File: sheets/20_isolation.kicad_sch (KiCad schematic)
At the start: 0 parts

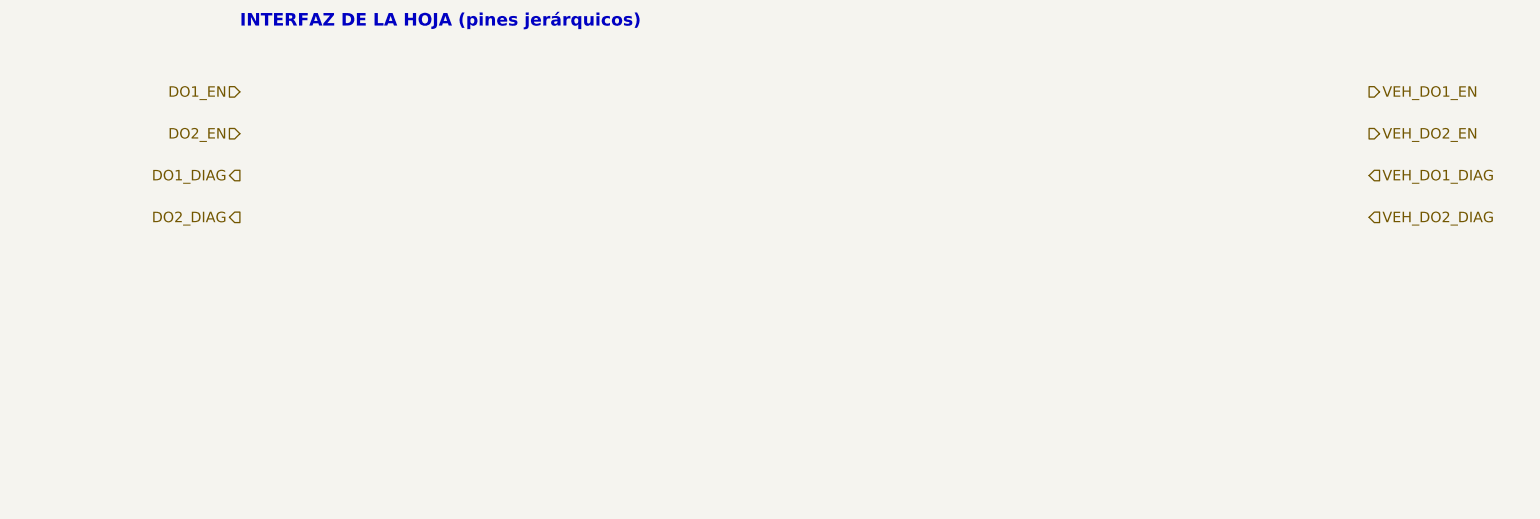
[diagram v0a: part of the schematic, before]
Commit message: 70_output: salida low-side con latch y señal PWR_FLT
- 70_output (DO1/DO2): MOSFET FDD7N25LZ (demo, 250 V) con TVS SMCJ188A
  en el drenador, latch de sobrecorriente a ~0.7 A (R 1 ohm + BC817/BC807,
  rearme con EN=0), apagado del gate por PWR_FLT_N o latch (BAT54A) y
  DIAG por divisor del drenador con zener 5V1. OUT pasa a pasivo.
- Jerarquía: VEH_PWR_FLT_N de 10_power_input a 70_output y 20_isolation;
  PWR_FLT de 20_isolation a 40_mcu (KW45 y ESP32-S3).
- 10_power_input: solo interfaz (VEH_DO1/2 pasivos, VEH_PWR_FLT_N);
  el circuito con LM74930 va en un commit aparte.
- CLAUDE.md: procedimiento para componentes fuera de las librerías.
- README: 70_output es low-side.

Co-Authored-By: Claude Opus 5.5 <noreply@anthropic.com>
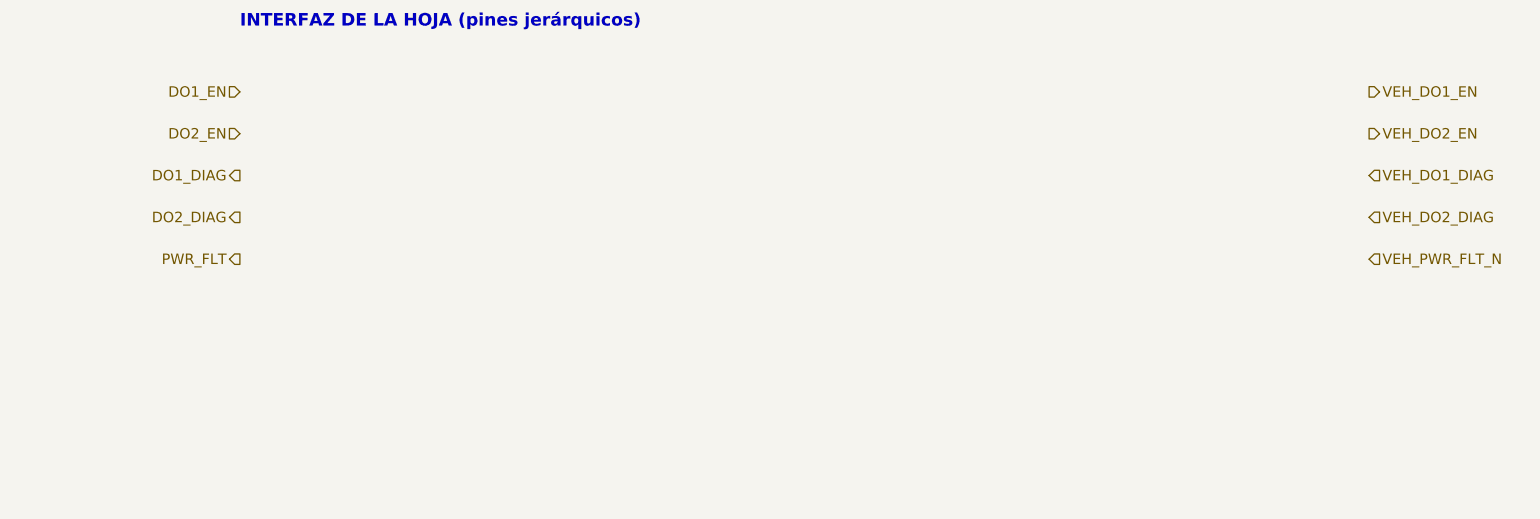
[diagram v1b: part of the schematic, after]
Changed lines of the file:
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@@
+		)
+	)
+	(hierarchical_label "VEH_PWR_FLT_N"
+		(shape input)
+		(at 375.92 50.8 0)
+		(effects
+			(font
+				(size 1.27 1.27)
+			)
+			(justify left)
+		)
+	)
+	(hierarchical_label "PWR_FLT"
+		(shape output)
+		(at 238.76 50.8 180)
+		(effects
+			(font
+				(size 1.27 1.27)
+			)
+			(justify right)
 		)
 	)

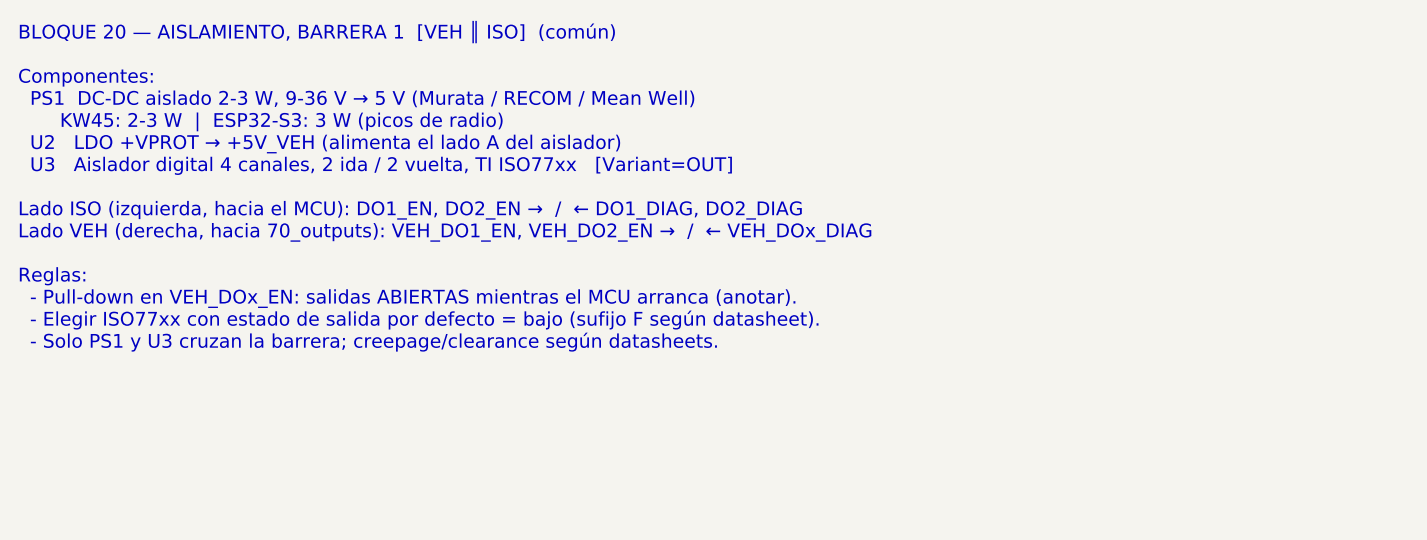
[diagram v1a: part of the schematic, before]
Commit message: Alcance: solo ESP32-S3, CAN clásico por TWAI, sin MCP2518FD
- Raíz: el bloque 40_mcu apunta a 40_mcu_esp32s3. 40_mcu_kw45 queda en
  el repo solo como referencia, fuera de la jerarquía.
- CAN: se eliminan el MCP2518FD, el cristal y los pines CANFD_SCK/MOSI/
  MISO, CS_CAN e INT_CAN en 60_can, 40_mcu_esp32s3 y la raíz (etiquetas,
  cables y pines de hoja). TWAI nativo (J1939) directo al ADM3055E.
  Se quita la variante CANFD.
- 20_isolation (nota): PS1 >= 5 W y entrada 9-72 V (corte OV 38.4 V);
  U2 = TPS7A1650-Q1 para +5V_VEH.
- 40_mcu_esp32s3 (nota): desacople 22 uF + 100 nF según Espressif y
  límite de 47 uF en +3V3_D por el TPS62A02-Q1; solo BLE en operación.
- README: tabla corregida (LM74930-Q1 en 10_power_input, 20, 30, 40, 60),
  sección MCU y "Requisitos para el firmware" (rearme del latch >= 100 ms,
  arranque limpio tras brownout, NimBLE con WiFi desactivado).
- CLAUDE.md: sección "Alcance" (ESP32-S3 único, dimensionar con WiFi).

ERC: 180 -> 160 violaciones; sin errores nuevos. Las restantes son de
hojas sin terminar (20, 30, 60) y etiquetas de la raíz sin destino.

Co-Authored-By: Claude Opus 5.5 <noreply@anthropic.com>
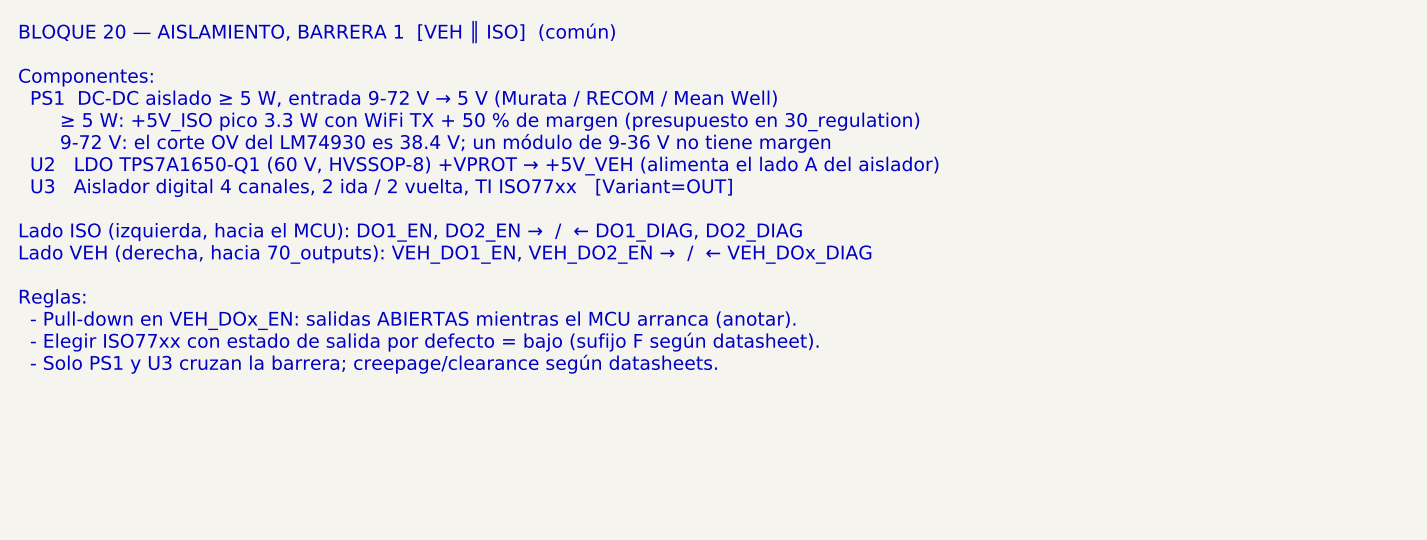
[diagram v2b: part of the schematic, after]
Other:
- note added: "BLOQUE 20 — AISLAMIENTO, BARRERA 1 [VEH ║ ISO] (común) Componentes: PS1 DC-DC aislado ≥ 5 W, entrada 9-72 V → 5 V (Murata / RECOM / Mean Well) ≥ 5 W: +5V_ISO pico 3.3 W con WiFi TX + 50 % de margen (presupuesto en 30_regulation) 9-72 V: el corte OV del LM74930 es 38.4 V; un módulo de 9-36 V no tiene margen U2 LDO TPS7A1650-Q1 (60 V, HVSSOP-8) +VPROT → +5V_VEH (alimenta el lado A del aislador) U3 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"
- note removed: "BLOQUE 20 — AISLAMIENTO, BARRERA 1 [VEH ║ ISO] (común) Componentes: PS1 DC-DC aislado 2-3 W, 9-36 V → 5 V (Murata / RECOM / Mean Well) KW45: 2-3 W | ESP32-S3: 3 W (picos de radio) U2 LDO +VPROT → +5V_VEH (alimenta el lado A del aislador) U3 Aislador digital 4 canales, 2 ida / 2 vuelta, TI ISO77xx [Variant=OUT] Lado ISO (izquierda, hacia el MCU): DO1_EN, DO2_EN → / ← DO1_DIAG, DO2_DIAG Lado VEH (d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"
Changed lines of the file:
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@@
 		)
 	)
-	(text "BLOQUE 20 — AISLAMIENTO, BARRERA 1  [VEH ║ ISO]  (común)\n\nComponentes:\n  PS1  DC-DC aislado 2-3 W, 9-36 V → 5 V (Murata / RECOM / Mean Well)\n       KW45: 2-3 W  |  ESP32-S3: 3 W (picos de radio)\n  U2   LDO +VPROT → +5V_VEH (alimenta el lado A del aislador)\n  U3   Aislador digital 4 canales, 2 ida / 2 vuelta, TI ISO77xx   [Variant=OUT]\n\nLado ISO (izquierda, hacia el MCU): DO1_EN, DO2_EN →  /  ← DO1_DIAG, DO2_DIAG\nLado VEH (derecha, hacia 70_outputs): VEH_DO1_EN, VEH_DO2_EN →  /  ← VEH_DOx_DIAG\n\nReglas:\n  - Pull-down en VEH_DOx_EN: salidas ABIERTAS mientras el MCU arranca (anotar).\n  - Elegir ISO77xx con estado de salida por defecto = bajo (sufijo F según datasheet).\n  - Solo PS1 y U3 cruzan la barrera; creepage/clearance según datasheets."
+	(text "BLOQUE 20 — AISLAMIENTO, BARRERA 1  [VEH ║ ISO]  (común)\n\nComponentes:\n  PS1  DC-DC aislado ≥ 5 W, entrada 9-72 V → 5 V (Murata / RECOM / Mean Well)\n       ≥ 5 W: +5V_ISO pico 3.3 W con WiFi TX + 50 % de margen (presupuesto en 30_regulation)\n       9-72 V: el corte OV del LM74930 es 38.4 V; un módulo de 9-36 V no tiene margen\n  U2   LDO TPS7A1650-Q1 (60 V, HVSSOP-8) +VPROT → +5V_VEH (alimenta el lado A del aislador)\n  U3   Aislador digital 4 canales, 2 ida / 2 vuelta, TI ISO77xx   [Variant=OUT]\n\nLado ISO (izquierda, hacia el MCU): DO1_EN, DO2_EN →  /  ← DO1_DIAG, DO2_DIAG\nLado VEH (derecha, hacia 70_outputs): VEH_DO1_EN, VEH_DO2_EN →  /  ← VEH_DOx_DIAG\n\nReglas:\n  - Pull-down en VEH_DOx_EN: salidas ABIERTAS mientras el MCU arranca (anotar).\n  - Elegir ISO77xx con estado de salida por defecto = bajo (sufijo F según datasheet).\n  - Solo PS1 y U3 cruzan la barrera; creepage/clearance según datasheets."
 		(exclude_from_sim no)
 		(at 20.32 20.32 0)
@@
 		)
 	)
+	(hierarchical_label "PWR_FLT"
+		(shape output)
+		(at 238.76 50.8 180)
+		(effects
+			(font
+				(size 1.27 1.27)
+			)
+			(justify right)
+		)
+	)
 	(hierarchical_label "DO2_EN"
 		(shape input)
@@
 		(shape input)
 		(at 375.92 40.64 0)
+		(effects
+			(font
+				(size 1.27 1.27)
+			)
+			(justify left)
+		)
+	)
+	(hierarchical_label "VEH_PWR_FLT_N"
+		(shape input)
+		(at 375.92 50.8 0)
 		(effects
 			(font
@@
 		)
 	)
-	(hierarchical_label "VEH_PWR_FLT_N"
-		(shape input)
-		(at 375.92 50.8 0)
-		(effects
-			(font
-				(size 1.27 1.27)
-			)
-			(justify left)
-		)
-	)
-	(hierarchical_label "PWR_FLT"
-		(shape output)
-		(at 238.76 50.8 180)
-		(effects
-			(font
-				(size 1.27 1.27)
-			)
-			(justify right)
-		)
-	)

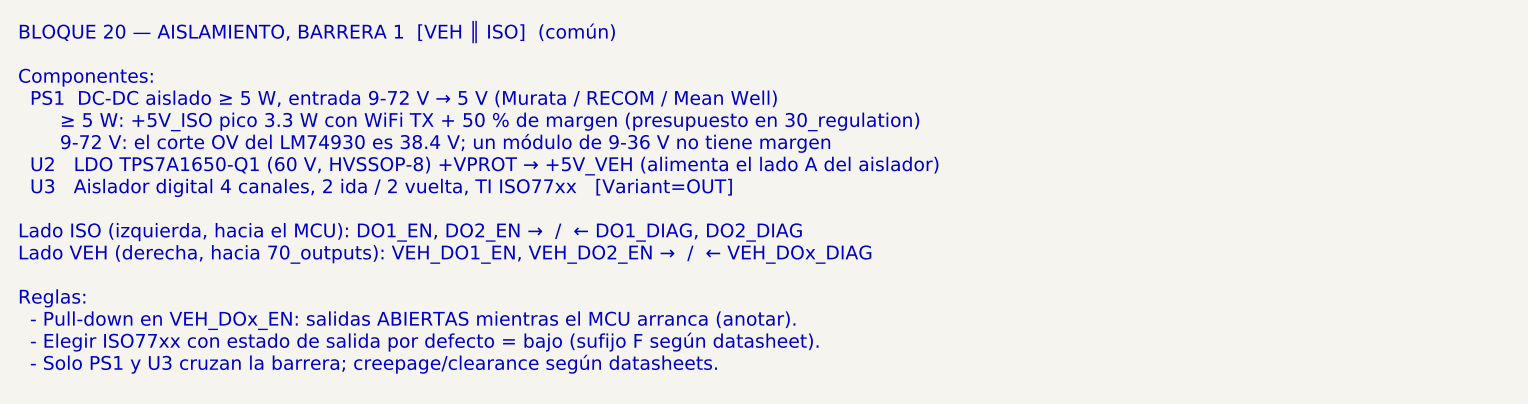
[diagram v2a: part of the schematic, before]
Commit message: ADM3055E: consumo de VCC confirmado con el datasheet Rev. D
- ICC en dominante con RL = 60 ohm: 180 mA típ / 260 mA máx (tabla 1);
  IIO 3.6 / 5 mA. Anotado en 60_can.
- +5V_ISO pico: 0.26 A (ADM3055E) + 0.39 A (buck, 521 mA en +3V3_D con
  WiFi TX) + 0.02 A (LDO) = 3.35 W; x1.5 = 5.0 W. PS1 se mantiene en
  >= 5 W (no hace falta 6 W). Nota de 20_isolation actualizada.
- docs/datasheets/adm3055e-adm3057e.pdf.

Co-Authored-By: Claude Opus 5.5 <noreply@anthropic.com>
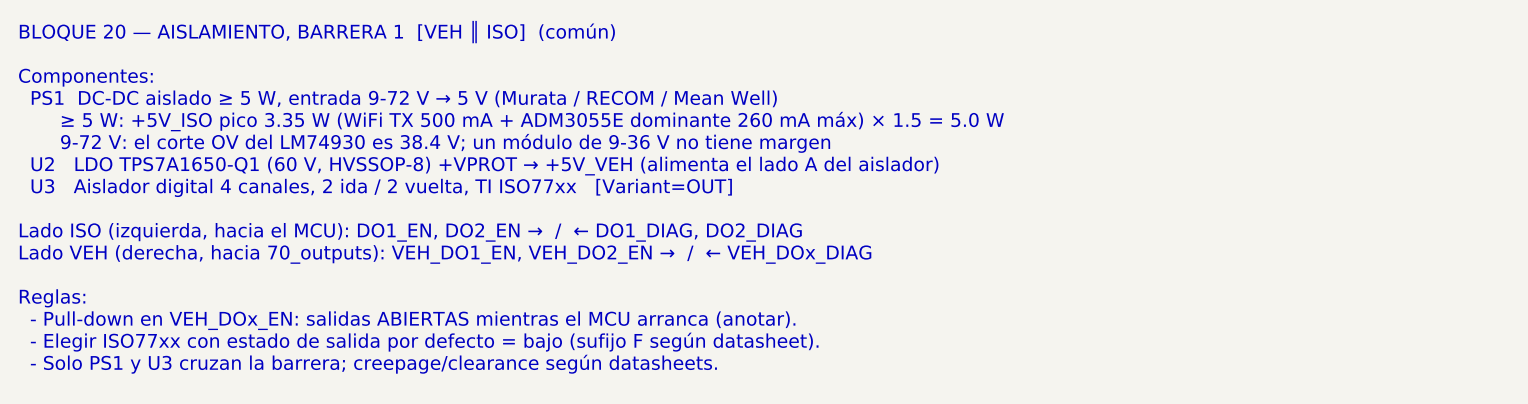
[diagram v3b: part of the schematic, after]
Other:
- note added: "BLOQUE 20 — AISLAMIENTO, BARRERA 1 [VEH ║ ISO] (común) Componentes: PS1 DC-DC aislado ≥ 5 W, entrada 9-72 V → 5 V (Murata / RECOM / Mean Well) ≥ 5 W: +5V_ISO pico 3.35 W (WiFi TX 500 mA + ADM3055E dominante 260 mA máx) × 1.5 = 5.0 W 9-72 V: el corte OV del LM74930 es 38.4 V; un módulo de 9-36 V no tiene margen U2 LDO TPS7A1650-Q1 (60 V, HVSSOP-8) +VPROT → +5V_VEH (alimenta el lado A del aislador)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"
- note removed: "BLOQUE 20 — AISLAMIENTO, BARRERA 1 [VEH ║ ISO] (común) Componentes: PS1 DC-DC aislado ≥ 5 W, entrada 9-72 V → 5 V (Murata / RECOM / Mean Well) ≥ 5 W: +5V_ISO pico 3.3 W con WiFi TX + 50 % de margen (presupuesto en 30_regulation) 9-72 V: el corte OV del LM74930 es 38.4 V; un módulo de 9-36 V no tiene margen U2 LDO TPS7A1650-Q1 (60 V, HVSSOP-8) +VPROT → +5V_VEH (alimenta el lado A del aislador) U3 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"
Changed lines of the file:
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@@
 		)
 	)
-	(text "BLOQUE 20 — AISLAMIENTO, BARRERA 1  [VEH ║ ISO]  (común)\n\nComponentes:\n  PS1  DC-DC aislado ≥ 5 W, entrada 9-72 V → 5 V (Murata / RECOM / Mean Well)\n       ≥ 5 W: +5V_ISO pico 3.3 W con WiFi TX + 50 % de margen (presupuesto en 30_regulation)\n       9-72 V: el corte OV del LM74930 es 38.4 V; un módulo de 9-36 V no tiene margen\n  U2   LDO TPS7A1650-Q1 (60 V, HVSSOP-8) +VPROT → +5V_VEH (alimenta el lado A del aislador)\n  U3   Aislador digital 4 canales, 2 ida / 2 vuelta, TI ISO77xx   [Variant=OUT]\n\nLado ISO (izquierda, hacia el MCU): DO1_EN, DO2_EN →  /  ← DO1_DIAG, DO2_DIAG\nLado VEH (derecha, hacia 70_outputs): VEH_DO1_EN, VEH_DO2_EN →  /  ← VEH_DOx_DIAG\n\nReglas:\n  - Pull-down en VEH_DOx_EN: salidas ABIERTAS mientras el MCU arranca (anotar).\n  - Elegir ISO77xx con estado de salida por defecto = bajo (sufijo F según datasheet).\n  - Solo PS1 y U3 cruzan la barrera; creepage/clearance según datasheets."
+	(text "BLOQUE 20 — AISLAMIENTO, BARRERA 1  [VEH ║ ISO]  (común)\n\nComponentes:\n  PS1  DC-DC aislado ≥ 5 W, entrada 9-72 V → 5 V (Murata / RECOM / Mean Well)\n       ≥ 5 W: +5V_ISO pico 3.35 W (WiFi TX 500 mA + ADM3055E dominante 260 mA máx) × 1.5 = 5.0 W\n       9-72 V: el corte OV del LM74930 es 38.4 V; un módulo de 9-36 V no tiene margen\n  U2   LDO TPS7A1650-Q1 (60 V, HVSSOP-8) +VPROT → +5V_VEH (alimenta el lado A del aislador)\n  U3   Aislador digital 4 canales, 2 ida / 2 vuelta, TI ISO77xx   [Variant=OUT]\n\nLado ISO (izquierda, hacia el MCU): DO1_EN, DO2_EN →  /  ← DO1_DIAG, DO2_DIAG\nLado VEH (derecha, hacia 70_outputs): VEH_DO1_EN, VEH_DO2_EN →  /  ← VEH_DOx_DIAG\n\nReglas:\n  - Pull-down en VEH_DOx_EN: salidas ABIERTAS mientras el MCU arranca (anotar).\n  - Elegir ISO77xx con estado de salida por defecto = bajo (sufijo F según datasheet).\n  - Solo PS1 y U3 cruzan la barrera; creepage/clearance según datasheets."
 		(exclude_from_sim no)
 		(at 20.32 20.32 0)
